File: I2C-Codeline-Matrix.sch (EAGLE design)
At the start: 12 parts, among them CON1 CONNECTOR-I2CLEFT, CON2 CONNECTOR-I2CLEFT, CON3 CONNECTOR-GROVE-4P-2.0-347013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, CON4 CONNECTOR-GROVE-4P-2.0-347013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

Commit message: 2.1
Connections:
- net GND: now also MATRIX2.G@2
- net VCCIO: now also MATRIX2.V+@2
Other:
- note added: "2.1"
- note removed: "2.0"

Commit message: added values for connectors
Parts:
- JP1, JP2, JP3: value (none) -> 0.100
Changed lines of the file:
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@@
 <part name="CON4" library="SPCoast" deviceset="CONNECTOR-GROVE-4P-2.0" device="-3470130P1"/>
 <part name="V3" library="supply2" deviceset="GND" device=""/>
-<part name="JP1" library="SPCoast" deviceset="JUMPER-2" device="PTH_LOCK"/>
-<part name="JP2" library="SPCoast" deviceset="JUMPER-2" device="PTH_LOCK"/>
-<part name="JP3" library="SPCoast" deviceset="JUMPER-2" device="PTH_LOCK"/>
+<part name="JP1" library="SPCoast" deviceset="JUMPER-2" device="PTH_LOCK" value="0.100"/>
+<part name="JP2" library="SPCoast" deviceset="JUMPER-2" device="PTH_LOCK" value="0.100"/>
+<part name="JP3" library="SPCoast" deviceset="JUMPER-2" device="PTH_LOCK" value="0.100"/>
 <part name="V4" library="supply2" deviceset="GND" device=""/>
 <part name="VCC5" library="supply1" deviceset="VCCIO" device=""/>

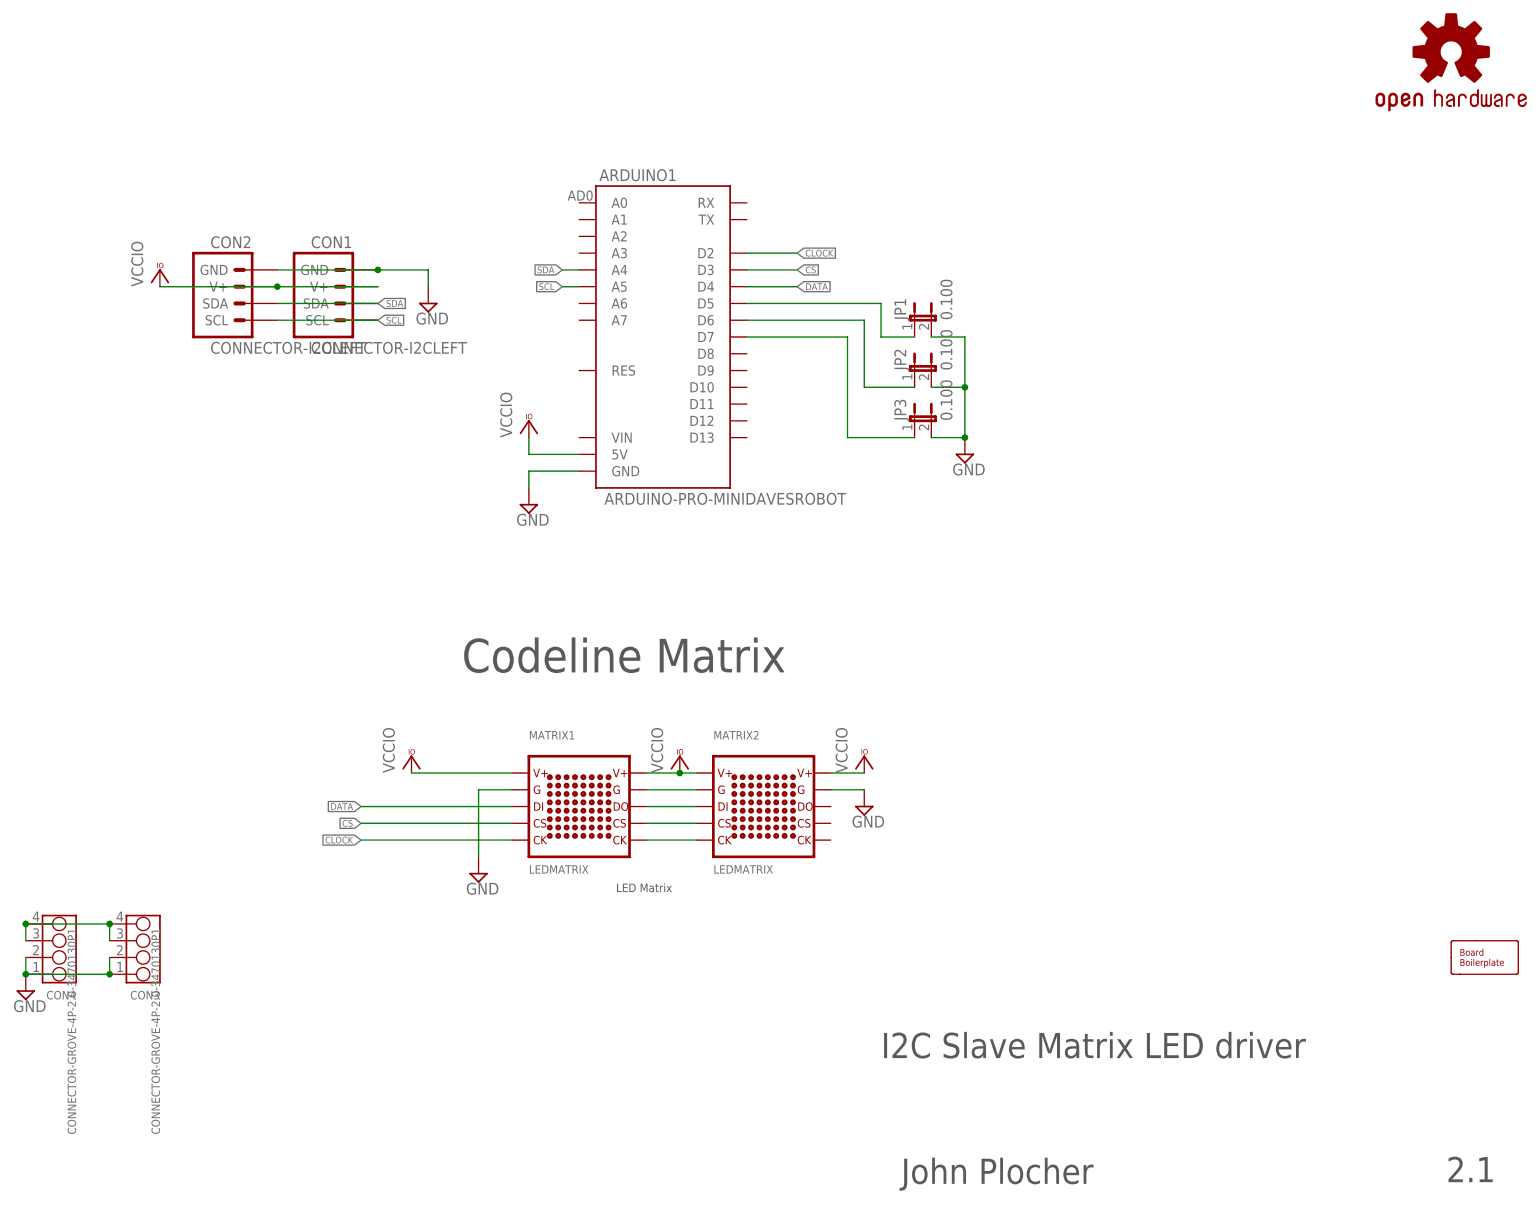
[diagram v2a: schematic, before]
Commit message: normalized values
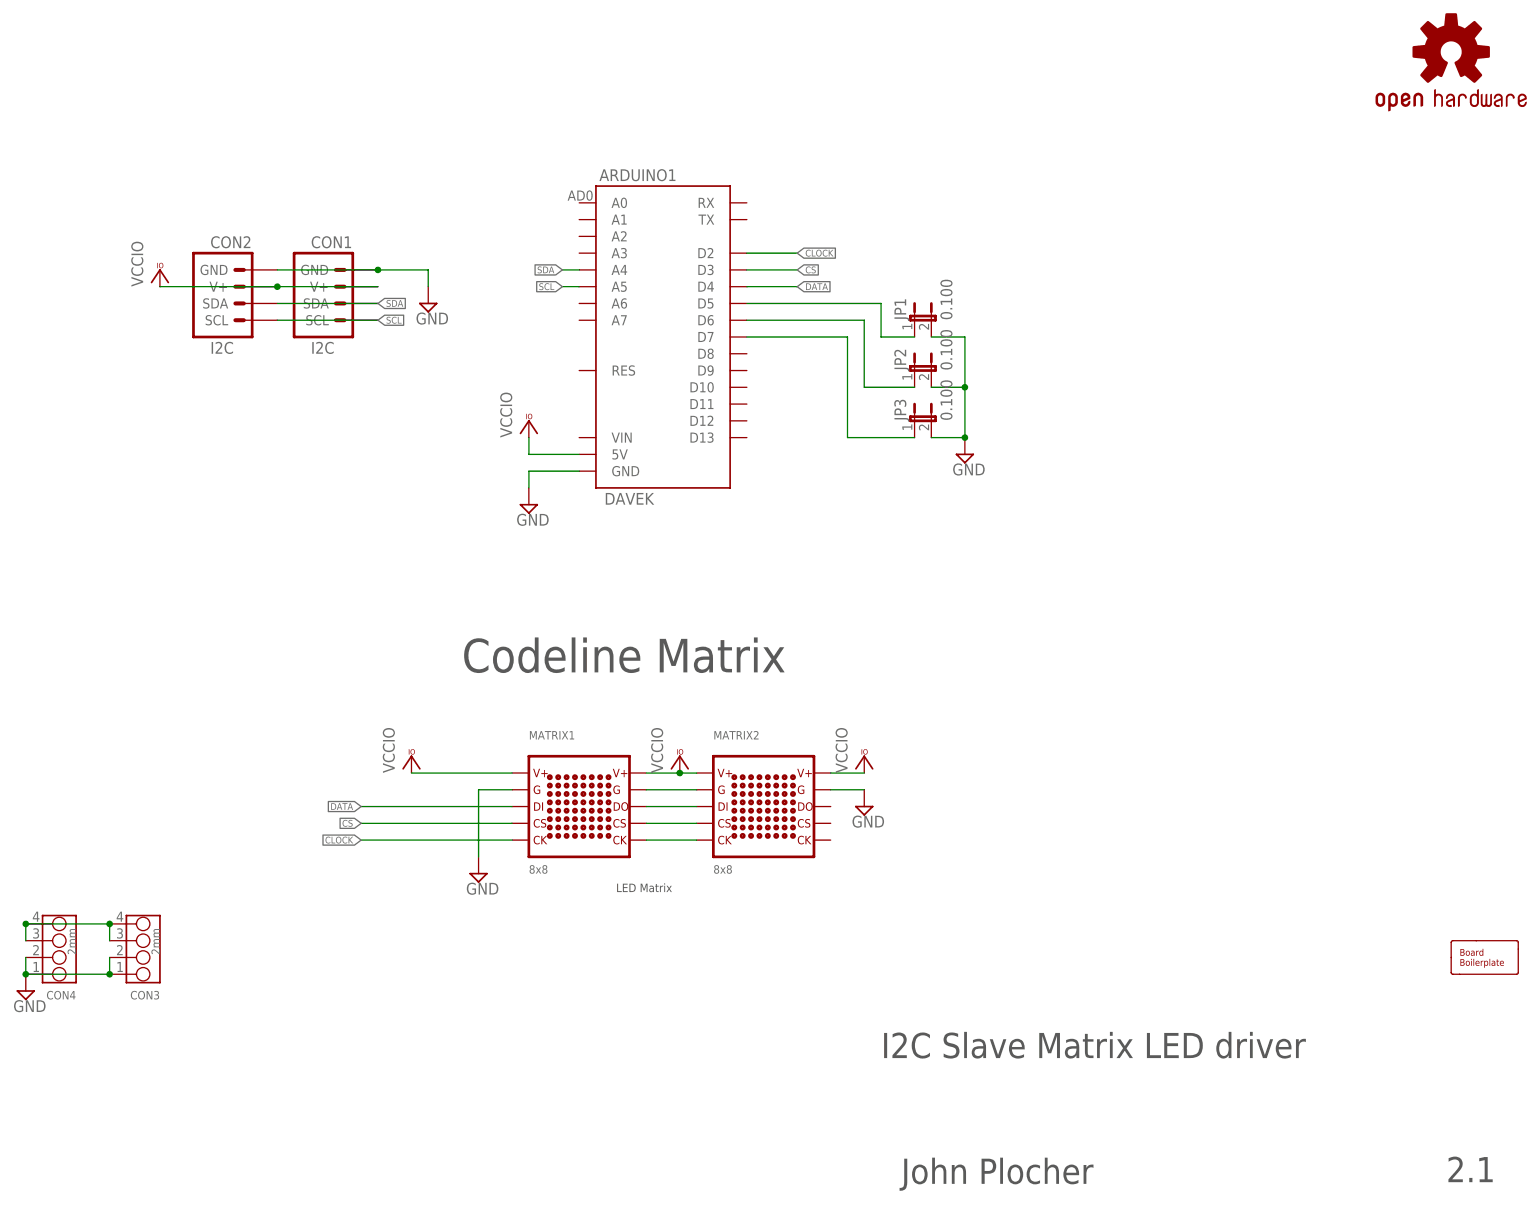
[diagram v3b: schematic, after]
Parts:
- ARDUINO1: value ARDUINO-PRO-MINIDAVESROBOT -> DAVEK
- BOARD: value BOARD80X150 -> BOARD
- CON1, CON2: value CONNECTOR-I2CLEFT -> I2C
- CON3, CON4: value CONNECTOR-GROVE-4P-2.0-3470130P1 -> 2mm
- MATRIX1, MATRIX2: value LEDMATRIX -> 8x8
- OSHW1: value OSHW-LOGOL -> OSHW
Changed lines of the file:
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@@
 <parts>
 <part name="FRAME1" library="MCP" deviceset="FRAME-LETTER" device=""/>
-<part name="OSHW1" library="SparkFun" deviceset="OSHW-LOGO" device="L" value="OSHW-LOGOL"/>
-<part name="BOARD" library="SPCoast" deviceset="BOARD" device="80X80-NOHOLES" value="BOARD80X150"/>
-<part name="MATRIX1" library="SPCoast" deviceset="LEDMATRIX" device=""/>
-<part name="MATRIX2" library="SPCoast" deviceset="LEDMATRIX" device=""/>
+<part name="OSHW1" library="SparkFun" deviceset="OSHW-LOGO" device="L" value="OSHW"/>
+<part name="BOARD" library="SPCoast" deviceset="BOARD" device="80X80-NOHOLES" value="BOARD"/>
+<part name="MATRIX1" library="SPCoast" deviceset="LEDMATRIX" device="" value="8x8"/>
+<part name="MATRIX2" library="SPCoast" deviceset="LEDMATRIX" device="" value="8x8"/>
 <part name="VCC2" library="supply1" deviceset="VCCIO" device=""/>
 <part name="V6" library="supply2" deviceset="GND" device=""/>
-<part name="ARDUINO1" library="SPCoast" deviceset="ARDUINO-PRO-MINI" device="DAVESROBOT"/>
-<part name="CON1" library="SPCoast" deviceset="CONNECTOR-I2C" device="LEFT"/>
-<part name="CON2" library="SPCoast" deviceset="CONNECTOR-I2C" device="LEFT"/>
+<part name="ARDUINO1" library="SPCoast" deviceset="ARDUINO-PRO-MINI" device="DAVESROBOT" value="DAVEK"/>
+<part name="CON1" library="SPCoast" deviceset="CONNECTOR-I2C" device="LEFT" value="I2C"/>
+<part name="CON2" library="SPCoast" deviceset="CONNECTOR-I2C" device="LEFT" value="I2C"/>
 <part name="VCC3" library="supply1" deviceset="VCCIO" device=""/>
 <part name="V2" library="supply2" deviceset="GND" device=""/>
 <part name="VCC1" library="supply1" deviceset="VCCIO" device=""/>
 <part name="V1" library="supply2" deviceset="GND" device=""/>
-<part name="CON3" library="SPCoast" deviceset="CONNECTOR-GROVE-4P-2.0" device="-3470130P1"/>
-<part name="CON4" library="SPCoast" deviceset="CONNECTOR-GROVE-4P-2.0" device="-3470130P1"/>
+<part name="CON3" library="SPCoast" deviceset="CONNECTOR-GROVE-4P-2.0" device="-3470130P1" value="2mm"/>
+<part name="CON4" library="SPCoast" deviceset="CONNECTOR-GROVE-4P-2.0" device="-3470130P1" value="2mm"/>
 <part name="V3" library="supply2" deviceset="GND" device=""/>
 <part name="JP1" library="SPCoast" deviceset="JUMPER-2" device="PTH_LOCK" value="0.100"/>
@@
 <instance part="FRAME1" gate="G$2" x="147.32" y="0"/>
 <instance part="OSHW1" gate="G$1" x="236.22" y="177.8"/>
-<instance part="BOARD" gate="G$1" x="241.3" y="40.64"/>
+<instance part="BOARD" gate="B" x="241.3" y="40.64"/>
 <instance part="MATRIX1" gate="1" x="104.14" y="63.5"/>
 <instance part="MATRIX2" gate="1" x="132.08" y="63.5"/>
 <instance part="VCC2" gate="G$1" x="78.74" y="71.12"/>
 <instance part="V6" gate="GND" x="88.9" y="53.34"/>
-<instance part="ARDUINO1" gate="G$1" x="116.84" y="134.62"/>
+<instance part="ARDUINO1" gate="A" x="116.84" y="134.62"/>
 <instance part="CON1" gate="I2C" x="66.04" y="142.24"/>
 <instance part="CON2" gate="I2C" x="50.8" y="142.24"/>
@@
 </segment>
 <segment>
-<pinref part="ARDUINO1" gate="G$1" pin="GND"/>
+<pinref part="ARDUINO1" gate="A" pin="GND"/>
 <wire x1="104.14" y1="114.3" x2="96.52" y2="114.3" width="0.1524" layer="91"/>
 <wire x1="96.52" y1="114.3" x2="96.52" y2="111.76" width="0.1524" layer="91"/>
@@
 </segment>
 <segment>
-<pinref part="ARDUINO1" gate="G$1" pin="5V"/>
+<pinref part="ARDUINO1" gate="A" pin="5V"/>
 <wire x1="104.14" y1="116.84" x2="96.52" y2="116.84" width="0.1524" layer="91"/>
 <wire x1="96.52" y1="116.84" x2="96.52" y2="119.38" width="0.1524" layer="91"/>
@@
 </segment>
 <segment>
-<pinref part="ARDUINO1" gate="G$1" pin="D3"/>
+<pinref part="ARDUINO1" gate="A" pin="D3"/>
 <wire x1="129.54" y1="144.78" x2="137.16" y2="144.78" width="0.1524" layer="91"/>
 <label x="137.16" y="144.78" size="1.016" layer="95" xref="yes"/>
@@
 </segment>
 <segment>
-<pinref part="ARDUINO1" gate="G$1" pin="D4"/>
+<pinref part="ARDUINO1" gate="A" pin="D4"/>
 <wire x1="129.54" y1="142.24" x2="137.16" y2="142.24" width="0.1524" layer="91"/>
 <label x="137.16" y="142.24" size="1.016" layer="95" xref="yes"/>
@@
 </segment>
 <segment>
-<pinref part="ARDUINO1" gate="G$1" pin="D2"/>
+<pinref part="ARDUINO1" gate="A" pin="D2"/>
 <wire x1="129.54" y1="147.32" x2="137.16" y2="147.32" width="0.1524" layer="91"/>
 <label x="137.16" y="147.32" size="1.016" layer="95" xref="yes"/>
@@
 <net name="SCL" class="0">
 <segment>
-<pinref part="ARDUINO1" gate="G$1" pin="A5"/>
+<pinref part="ARDUINO1" gate="A" pin="A5"/>
 <wire x1="104.14" y1="142.24" x2="101.6" y2="142.24" width="0.1524" layer="91"/>
 <label x="101.6" y="142.24" size="1.016" layer="95" rot="R180" xref="yes"/>
@@
 <net name="SDA" class="0">
 <segment>
-<pinref part="ARDUINO1" gate="G$1" pin="A4"/>
+<pinref part="ARDUINO1" gate="A" pin="A4"/>
 <wire x1="104.14" y1="144.78" x2="101.6" y2="144.78" width="0.1524" layer="91"/>
 <label x="101.6" y="144.78" size="1.016" layer="95" rot="R180" xref="yes"/>
@@
 <net name="N$6" class="0">
 <segment>
-<pinref part="ARDUINO1" gate="G$1" pin="D5"/>
+<pinref part="ARDUINO1" gate="A" pin="D5"/>
 <wire x1="129.54" y1="139.7" x2="149.86" y2="139.7" width="0.1524" layer="91"/>
 <wire x1="149.86" y1="139.7" x2="149.86" y2="134.62" width="0.1524" layer="91"/>
@@
 <net name="N$7" class="0">
 <segment>
-<pinref part="ARDUINO1" gate="G$1" pin="D6"/>
+<pinref part="ARDUINO1" gate="A" pin="D6"/>
 <wire x1="129.54" y1="137.16" x2="147.32" y2="137.16" width="0.1524" layer="91"/>
 <wire x1="147.32" y1="137.16" x2="147.32" y2="127" width="0.1524" layer="91"/>
@@
 <net name="N$8" class="0">
 <segment>
-<pinref part="ARDUINO1" gate="G$1" pin="D7"/>
+<pinref part="ARDUINO1" gate="A" pin="D7"/>
 <wire x1="129.54" y1="134.62" x2="144.78" y2="134.62" width="0.1524" layer="91"/>
 <wire x1="144.78" y1="134.62" x2="144.78" y2="119.38" width="0.1524" layer="91"/>
